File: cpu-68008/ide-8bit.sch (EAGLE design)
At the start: 62 parts, among them IC101 GAL22V10D, IC102 74HCT175N, IC201 YM3812, IC202 YM3014B, IC203 AY-3-8910, IC301 TL062, IC302 TL062, IC401 74HCT14N, IC402 SCC2691, J301 RCALOCK, J401 DIN5, J402 DIN5, Q401 3MHz

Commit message: Added 8-bit IDE board Finished routing of sound board
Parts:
- removed C105, C205, C404: 10µF, rcl:CPOL-EUSMCB
- removed C106, C107, C204, C304, C307, C401, C402, C403: 100nF, rcl:C-EUC0805
- removed C301, C302: 10µF, rcl:CPOL-EUE2-5
- removed C303: 220µF, rcl:CPOL-EUE2.5-6
- removed C305, C306: 4.7µF, rcl:CPOL-EUE2-5
- removed C405, C406: 27pF, rcl:C-EUC0805
- removed D401: 1N914, diode:1N4148DO35-10
- removed IC102: 74HCT175N, 74xx-eu:74HCT175N
- removed IC202: YM3014B, 68komputer:YM3014BDIL8
- removed IC203: AY-3-8910, 68komputer:AY-3-8910
- removed IC301, IC302: TL062, linear:TL062P
- removed IC401: 74HCT14N, 74xx-eu:74HCT14N
- removed IC402: SCC2691, 68komputer:SCC2691
- removed J301: RCALOCK, SparkFun-Connectors:RCALOCK
- removed J401, J402: DIN5, SparkFun-Connectors:DIN5
- removed OK401: H11L1M, optocoupler:H11L1M
- removed Q401: 3MHz, crystal:CRYSTALHC49S
- removed QG201: 3.579545 MHz, crystal:XO-14
- removed R301, R302, R303, R307, R308: 1k, rcl:R-EU_R2012
- removed R304, R309, R310, R402, R404: 4k7, rcl:R-EU_R2012
- removed R305, R306: 1k, pot:TRIM_EU-PT10S
- removed R311: 10k, pot:TRIM_EU-PT10S
- removed R401, R403: 220R, rcl:R-EU_R2012
- removed SV102, SV103: (no value), con-lstb:MA10-1
- removed SV104, SV105: (no value), con-lstb:MA05-2
- removed WEED401: WEED, 68komputer:WEED
- added LED201: (no value), led:LEDCHIPLED_1206
- added R201: 10k, rcl:R-EU_R2012
- added R202: 3k, rcl:R-EU_R2012
- added SV201: (no value), con-harting-ml:ML40L
- added SV202: (no value), con-lstb:MA04-1
- C104, C202: value 100nF -> 10µF; device rcl:C-EUC0805 -> rcl:CPOL-EUSMCB; MOUSER 710-885012207072 -> 581-TAJB106K020RNJV
- IC201: value YM3812 -> 74HCT245N; device 68komputer:YM3812DIL24 -> 74xx-eu:74HCT245N; MOUSER (none) -> 595-SN74HCT245N; MOUSER_SOCKET 575-1104762441001000 -> 575-1104732041001000
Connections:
- removed net !ACCESS_TIMER_CLEAR: IC101.IO23, IC102A.CLR
- removed net !AY_DONE: IC101.IN10, SV105.1, SV105.3, SV105.5, SV105.7, SV105.9
- removed net !DONE_1: IC102A.!Q1, SV104.10, SV105.10
- removed net !DONE_2: IC102A.!Q2, SV104.8, SV105.8
- removed net !DONE_3: IC102A.!Q3, SV104.6, SV105.6
- removed net !DONE_4: IC102A.!Q4, SV104.4, SV105.4
- removed net !MIDI_IRQ: IC101.IN9, IC402.!IRQ, R404.1
- removed net !MIDI_UART_CS: IC101.IO19, IC402.!CS
- removed net !RD: IC101.IO20, IC201.!RD, IC402.!RD
- removed net !YM_CS: IC101.IO21, IC201.!CS
- removed net !YM_DONE: IC101.IN11, SV104.1, SV104.3, SV104.5, SV104.7, SV104.9
- removed net !YM_IRQ: IC101.IN13, IC201.!IRQ
- removed net AUDIO: C303.+, IC302A.OUT, R311.S
- removed net AY_BC1: IC101.IO17, IC203.BC1
- removed net AY_BC2: IC101.IO16, IC203.BC2
- removed net AY_BDIR: IC101.IO15, IC203.BDIR
- removed net CLK_A: IC101.IN1/CLK, IC102A.CLK, IC201.CLK, IC203.CLK, QG201.OUT
- removed net FM_OUT: IC301A.-IN, IC301A.OUT, R305.E
- removed net IOA0: IC203.IOA0, SV102.1
- removed net IOA1: IC203.IOA1, SV102.2
- removed net IOA2: IC203.IOA2, SV102.3
- removed net IOA3: IC203.IOA3, SV102.4
- removed net IOA4: IC203.IOA4, SV102.5
- removed net IOA5: IC203.IOA5, SV102.6
- removed net IOA6: IC203.IOA6, SV102.7
- removed net IOA7: IC203.IOA7, SV102.8
- removed net IOB0: IC203.IOB0, SV103.1
- removed net IOB1: IC203.IOB1, SV103.2
- removed net IOB2: IC203.IOB2, SV103.3
- removed net IOB3: IC203.IOB3, SV103.4
- removed net IOB4: IC203.IOB4, SV103.5
- removed net IOB5: IC203.IOB5, SV103.6
- removed net IOB6: IC203.IOB6, SV103.7
- removed net IOB7: IC203.IOB7, SV103.8
- removed net MIDI_RESET: IC401C.O, IC402.RESET
- removed net MIDI_RX: IC402.RXD, OK401.OUT, R402.1
- removed net MIDI_RX_+: D401.A, J401.5, OK401.C
- removed net MIDI_RX_-: D401.C, OK401.A, R401.2
- removed net MIDI_TX: IC401A.I, IC402.TXD
- removed net MIDI_TX_-: IC401B.O, J402.5
- removed net MIDI_UART_X1: C405.2, IC402.X1/CLK, Q401.1
- removed net MIDI_UART_X2: C406.2, IC402.X2, Q401.2
- removed net N$1: C305.+, R305.S
- removed net N$10: C305.-, R307.1
- removed net N$11: C306.-, R308.1
- removed net N$12: IC302A.-IN, R307.2, R308.2, R311.A
- removed net N$13: IC302B.-IN, IC302B.OUT
- removed net N$14: J401.4, R401.1
- removed net N$15: IC302B.+IN, R309.2, R310.1
- removed net N$16: IC401A.O, IC401B.I
- removed net N$17: J402.4, R403.1
- removed net N$2: IC102A.D4, IC102A.Q3
- removed net N$4: C303.-, J301.PIN
- removed net N$5: IC102A.D2, IC102A.Q1
- removed net N$6: IC102A.D3, IC102A.Q2
- removed net PSG_OUT: R301.1, R302.1, R303.1, R304.2, R306.E
- removed net PSG_OUT_A: IC203.OUTA, R301.2
- removed net PSG_OUT_B: IC203.OUTB, R302.2
- removed net PSG_OUT_C: IC203.OUTC, R303.2
- removed net YM_DAC_CLK: IC201.DACCLK, IC202.CLK
- removed net YM_DAC_DATA: IC201.DACMO, IC202.DATA
- removed net YM_DAC_SY: IC201.DACSY, IC202.SYNC
- removed net YM_OUT_BUF: IC202.BUFF, IC301A.+IN
- removed net YM_OUT_MP: C301.+, IC202.MP, IC301B.-IN, IC301B.OUT
- removed net YM_OUT_RB: C302.+, IC202.RB, IC301B.+IN
- new net !ATA_ACTY: LED201.C, SV201.39
- new net !ATA_BUF_EN: IC101.IO18, IC201A.G
- new net !ATA_CS0: IC101.IO22, SV201.37
- new net !ATA_CS1: IC101.IO23, SV201.38
- new net !ATA_IRQ: IC101.IN2, R201.1, SV201.31
- new net ATA_D0: IC201A.B1, SV201.17
- new net ATA_D1: IC201A.B2, SV201.15
- new net ATA_D2: IC201A.B3, SV201.13
- new net ATA_D3: IC201A.B4, SV201.11
- new net ATA_D4: IC201A.B5, SV201.9
- new net ATA_D5: IC201A.B6, SV201.7
- new net ATA_D6: IC201A.B7, SV201.5
- new net ATA_D7: IC201A.B8, SV201.3
- new net ATA_DIR: IC101.IO19, IC201A.DIR
- new net ATA_IORD: IC101.IO21, SV201.25
- new net ATA_IORDY: IC101.IN3, SV201.27
- new net ATA_IOWR: IC101.IO20, SV201.23
- net !BUS_IRQ: now also IC101.IO15; no longer IC101.IO14
- net !RESET: now also SV201.1; no longer IC101.IO18, IC201.!RESET, IC203.!RESET, IC401C.I
- net !SLOT_ACK: now also IC101.IO14; no longer IC101.IO22
- net !SLOT_AS: now also IC101.IN7; no longer IC101.IN6
- net !SLOT_CS: now also IC101.IN13; no longer IC101.IN2
- net !SLOT_RESET: now also IC101.IN8; no longer IC101.IN5
- net +5V: now also C104.+, C202.+, IC201P.VCC, R201.2, R202.1, SV202.4; no longer C104.1, C105.+, C106.1, C107.1, C202.1, C204.1, C205.+, C304.1, C307.1, C401.1, C402.1, C403.1, C404.+, IC102A.D1, IC102P.VCC, IC201.VCC, IC202.VDD, IC203.A8, IC203.VCC, IC301P.V+, IC302P.V+, IC401P.VCC, IC402.VCC, OK401.VCC, QG201.VCC, R309.1, R402.2, R403.2, R404.2, SV102.9, SV103.9
- net GND: now also C104.-, C202.-, IC201P.GND, SV201.19, SV201.2, SV201.22, SV201.24, SV201.26, SV201.28, SV201.30, SV201.40, SV202.2, SV202.3; no longer C104.2, C105.-, C106.2, C107.2, C202.2, C204.2, C205.-, C301.-, C302.-, C304.2, C307.2, C401.2, C402.2, C403.2, C404.-, C405.1, C406.1, IC102P.GND, IC201.GND, IC202.GND, IC203.!A9, IC203.GND, IC301P.V-, IC302A.+IN, IC302P.V-, IC401D.I, IC401E.I, IC401F.I, IC401P.GND, IC402.GND, J301.SHELL, J402.2, OK401.GND, QG201.GND, R304.1, R305.A, R306.A, R310.2, SV102.10, SV103.10, SV104.2, SV105.2
- net N$7: now also LED201.A, R202.2; no longer C306.+, R306.S
- net SLOT_A0: now also SV201.35; no longer IC101.IN7, IC201.A0, IC402.A0
- net SLOT_A1: now also SV201.33; no longer IC402.A1
- net SLOT_A2: now also SV201.36; no longer IC402.A2
- net SLOT_A4: now also IC101.IN10
- net SLOT_A5: now also IC101.IN11
- net SLOT_A8: no longer IC101.IN3
- net SLOT_A9: no longer IC101.IN8
- net SLOT_D0: now also IC201A.A1; no longer IC201.D0, IC203.DA0, IC402.D0
- net SLOT_D1: now also IC201A.A2; no longer IC201.D1, IC203.DA1, IC402.D1
- net SLOT_D2: now also IC201A.A3; no longer IC201.D2, IC203.DA2, IC402.D2
- net SLOT_D3: now also IC201A.A4; no longer IC201.D3, IC203.DA3, IC402.D3
- net SLOT_D4: now also IC201A.A5; no longer IC201.D4, IC203.DA4, IC402.D4
- net SLOT_D5: now also IC201A.A6; no longer IC201.D5, IC203.DA5, IC402.D5
- net SLOT_D6: now also IC201A.A7; no longer IC201.D6, IC203.DA6, IC402.D6
- net SLOT_D7: now also IC201A.A8; no longer IC201.D7, IC203.DA7, IC402.D7
- net SLOT_R/!W!: now also IC101.IN9; no longer IC101.IN4, IC201.!WR, IC402.!WR
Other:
- note removed: "All resistors on this sheet should be ±1% or better"
- note removed: "CLK_A: 3.579545 MHz (YM) CLK_B: 2.0 MHz (AY, MIDI)"
- note removed: "CN401: MIDI In CN402: MIDI Out"
- note removed: "SV102/103 are connected to AY ports A/B Select wait states for YM3812/AY-3-8910 with SV104/105"
- note removed: "Select 38.4kBaud on IC402 for 31.25kBaud MIDI"
- note removed: "Unused"
- note removed: "YM2149F or YM3439 OK for IC204"

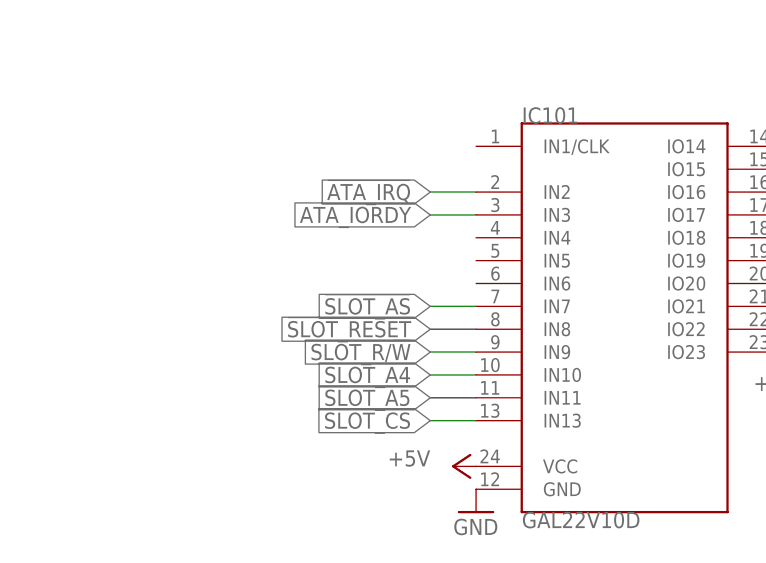
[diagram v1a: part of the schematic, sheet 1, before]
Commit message: added /DS to GALs on all peripherals and backplane began work on TMS9918 video card
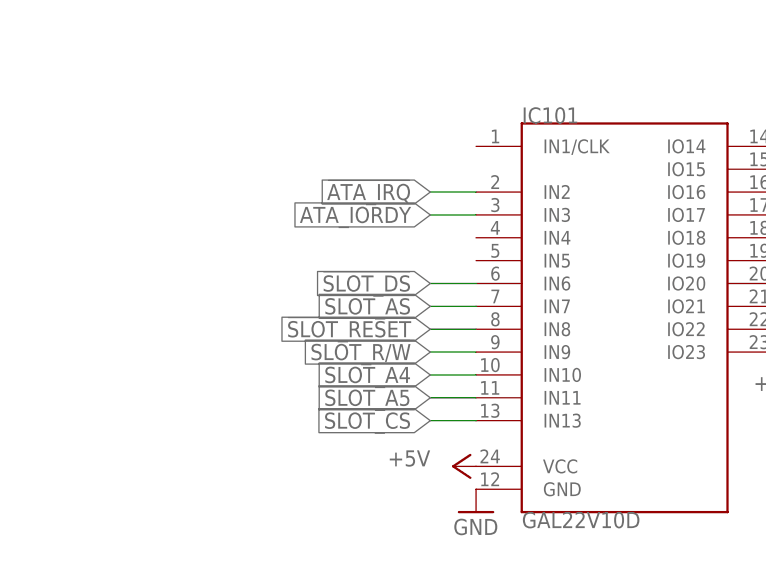
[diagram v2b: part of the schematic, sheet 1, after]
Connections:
- net !SLOT_DS: now also IC101.IN6
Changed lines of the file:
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@@
 <label x="25.4" y="162.56" size="1.778" layer="95" rot="R180" xref="yes"/>
+</segment>
+<segment>
+<pinref part="IC101" gate="G$1" pin="IN6"/>
+<wire x1="53.34" y1="33.02" x2="48.26" y2="33.02" width="0.1524" layer="91"/>
+<label x="48.26" y="33.02" size="1.778" layer="95" rot="R180" xref="yes"/>
 </segment>
 </net>

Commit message: minor revisions on mouser parts
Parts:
- added C1: 10µF, rcl:CPOL-EUSMCB
- added C2, C3, C4: 100nF, rcl:C-EUC0805
- added IC1: ATmega328P, SparkFun-IC-Microcontroller:ATMEGA328P_PDIP
- added SV1: (no value), con-harting-ml:ML6
- SV101: MOUSER (none) -> 517-30340-5002
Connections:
- new net !AVR_RESET: IC1.PC6(/RESET), SV1.2
- new net AVR_MISO: SV1.6
- new net AVR_MOSI: SV1.3
- new net AVR_SCK: SV1.4
- net +5V: now also C1.+, C2.1, C3.1, C4.1, IC1.AREF, IC1.AVCC, IC1.VCC, SV1.5
- net GND: now also C1.-, C2.2, C3.2, C4.2, IC1.GND, SV1.1
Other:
- note added: "SV301: AVR ISP header"
